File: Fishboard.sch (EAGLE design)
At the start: 21 parts, among them J3 B1, J4 B2, J5 B3, J7 B4, Q1 TIP120, Q2 TIP120, Q3 TIP120

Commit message: Reorganized schematics
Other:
- note added: "I2C Header for SSD1306"
- note added: "Input buttons"
- note added: "Oak Headers"
- note added: "Transistor Logic"
- moved on the sheet: J1, J10, J2, J4, J6, J8, J9, Q1, Q2, Q3, R1, R2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

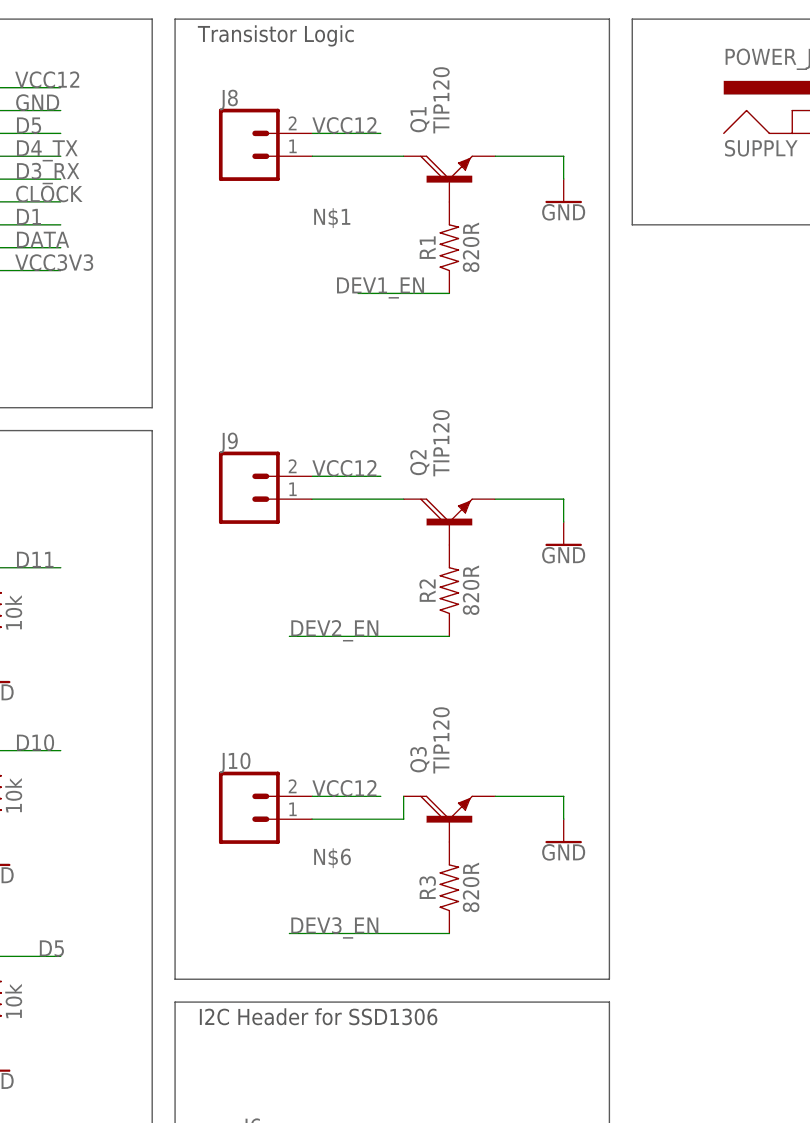
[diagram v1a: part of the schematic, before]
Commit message: Switched the TIP120 with a logic level MOSFET (FQP30N06L). The current limiting resistors have been replaced with pulldowns.
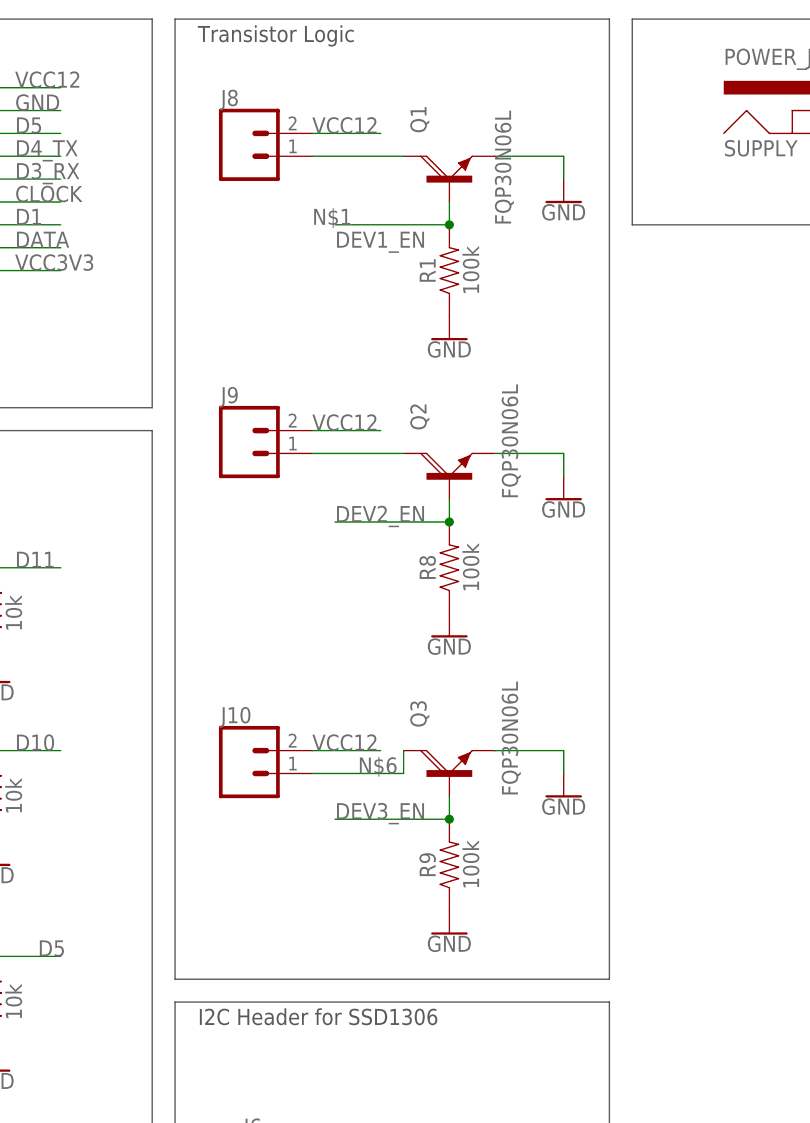
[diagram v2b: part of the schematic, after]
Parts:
- removed R2, R3: 820R, SparkFun-Resistors:1KOHM-HORIZ-1/4W-5%
- added R8, R9: 100k, SparkFun-Resistors:100KOHM-HORIZ-1/4W-5%
- Q1, Q2, Q3: value TIP120 -> FQP30N06L
- R1: value 820R -> 100k; device SparkFun-Resistors:1KOHM-HORIZ-1/4W-5% -> SparkFun-Resistors:100KOHM-HORIZ-1/4W-5%
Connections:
- removed net N$2: Q1.B, R1.2
- removed net N$3: Q2.B, R2.2
- removed net N$4: Q3.B, R3.2
- net DEV1_EN: now also Q1.B, R1.2; no longer R1.1
- net DEV2_EN: now also Q2.B, R8.2; no longer R2.1
- net DEV3_EN: now also Q3.B, R9.2; no longer R3.1
- net GND: now also R1.1, R8.1, R9.1
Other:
- moved on the sheet: J10, J9, Q2, Q3, R1
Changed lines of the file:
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@@
 <part name="GND1" library="SparkFun-PowerSymbols" deviceset="GND" device=""/>
 <part name="GND2" library="SparkFun-PowerSymbols" deviceset="GND" device=""/>
-<part name="Q1" library="transistor-power" deviceset="TIP120" device="" value="TIP120"/>
-<part name="Q2" library="transistor-power" deviceset="TIP120" device="" value="TIP120"/>
-<part name="Q3" library="transistor-power" deviceset="TIP120" device="" value="TIP120"/>
+<part name="Q1" library="transistor-power" deviceset="TIP120" device="" value="FQP30N06L"/>
+<part name="Q2" library="transistor-power" deviceset="TIP120" device="" value="FQP30N06L"/>
+<part name="Q3" library="transistor-power" deviceset="TIP120" device="" value="FQP30N06L"/>
 <part name="GND5" library="SparkFun-PowerSymbols" deviceset="GND" device=""/>
 <part name="GND6" library="SparkFun-PowerSymbols" deviceset="GND" device=""/>
-<part name="R1" library="SparkFun-Resistors" deviceset="1KOHM" device="-HORIZ-1/4W-5%" value="820R"/>
-<part name="R2" library="SparkFun-Resistors" deviceset="1KOHM" device="-HORIZ-1/4W-5%" value="820R"/>
-<part name="R3" library="SparkFun-Resistors" deviceset="1KOHM" device="-HORIZ-1/4W-5%" value="820R"/>
 <part name="J3" library="SparkFun-Connectors" deviceset="CONN_02" device="LOCK" value="B1"/>
 <part name="J4" library="SparkFun-Connectors" deviceset="CONN_02" device="LOCK" value="B2"/>
@@
 <part name="J9" library="SparkFun-Connectors" deviceset="CONN_02" device="PTH3"/>
 <part name="J10" library="SparkFun-Connectors" deviceset="CONN_02" device="PTH3"/>
+<part name="R1" library="SparkFun-Resistors" deviceset="100KOHM" device="-HORIZ-1/4W-5%" value="100k"/>
+<part name="R8" library="SparkFun-Resistors" deviceset="100KOHM" device="-HORIZ-1/4W-5%" value="100k"/>
+<part name="R9" library="SparkFun-Resistors" deviceset="100KOHM" device="-HORIZ-1/4W-5%" value="100k"/>
+<part name="GND9" library="SparkFun-PowerSymbols" deviceset="GND" device=""/>
+<part name="GND10" library="SparkFun-PowerSymbols" deviceset="GND" device=""/>
+<part name="GND11" library="SparkFun-PowerSymbols" deviceset="GND" device=""/>
 </parts>
 <sheets>
@@
 <instance part="GND1" gate="1" x="142.24" y="73.66"/>
 <instance part="GND2" gate="1" x="104.14" y="71.12"/>
-<instance part="Q1" gate="1" x="91.44" y="73.66" rot="R90"/>
-<instance part="Q2" gate="1" x="91.44" y="35.56" rot="R90"/>
-<instance part="Q3" gate="1" x="91.44" y="2.54" rot="R90"/>
-<instance part="GND5" gate="1" x="104.14" y="33.02"/>
-<instance part="GND6" gate="1" x="104.14" y="0"/>
-<instance part="R1" gate="G$1" x="91.44" y="66.04" rot="R90"/>
-<instance part="R2" gate="G$1" x="91.44" y="27.94" rot="R90"/>
-<instance part="R3" gate="G$1" x="91.44" y="-5.08" rot="R90"/>
+<instance part="Q1" gate="1" x="91.44" y="73.66" smashed="yes" rot="R90">
+<attribute name="NAME" x="88.9" y="78.74" size="1.778" layer="95" rot="R90"/>
+<attribute name="VALUE" x="96.52" y="81.28" size="1.778" layer="96" rot="R270"/>
+</instance>
+<instance part="Q2" gate="1" x="91.44" y="40.64" smashed="yes" rot="R90">
+<attribute name="NAME" x="88.9" y="45.72" size="1.778" layer="95" rot="R90"/>
+<attribute name="VALUE" x="99.06" y="38.1" size="1.778" layer="96" rot="R90"/>
+</instance>
+<instance part="Q3" gate="1" x="91.44" y="7.62" smashed="yes" rot="R90">
+<attribute name="NAME" x="88.9" y="12.7" size="1.778" layer="95" rot="R90"/>
+<attribute name="VALUE" x="99.06" y="5.08" size="1.778" layer="96" rot="R90"/>
+</instance>
+<instance part="GND5" gate="1" x="104.14" y="38.1"/>
+<instance part="GND6" gate="1" x="104.14" y="5.08"/>
 <instance part="J3" gate="G$1" x="10.16" y="27.94"/>
 <instance part="J4" gate="G$1" x="10.16" y="7.62"/>
@@
 <instance part="GND8" gate="1" x="40.64" y="-48.26"/>
 <instance part="J8" gate="G$1" x="68.58" y="76.2"/>
-<instance part="J9" gate="G$1" x="68.58" y="38.1"/>
-<instance part="J10" gate="G$1" x="68.58" y="2.54"/>
+<instance part="J9" gate="G$1" x="68.58" y="43.18"/>
+<instance part="J10" gate="G$1" x="68.58" y="7.62"/>
+<instance part="R1" gate="G$1" x="91.44" y="63.5" rot="R90"/>
+<instance part="R8" gate="G$1" x="91.44" y="30.48" rot="R90"/>
+<instance part="R9" gate="G$1" x="91.44" y="-2.54" rot="R90"/>
+<instance part="GND9" gate="1" x="91.44" y="55.88"/>
+<instance part="GND10" gate="1" x="91.44" y="22.86"/>
+<instance part="GND11" gate="1" x="91.44" y="-10.16"/>
 </instances>
 <busses>
@@
 <pinref part="Q2" gate="1" pin="E"/>
 <pinref part="GND5" gate="1" pin="GND"/>
-<wire x1="96.52" y1="38.1" x2="104.14" y2="38.1" width="0.1524" layer="91"/>
-<wire x1="104.14" y1="38.1" x2="104.14" y2="35.56" width="0.1524" layer="91"/>
+<wire x1="96.52" y1="43.18" x2="104.14" y2="43.18" width="0.1524" layer="91"/>
+<wire x1="104.14" y1="43.18" x2="104.14" y2="40.64" width="0.1524" layer="91"/>
 </segment>
 <segment>
@@
 <pinref part="Q3" gate="1" pin="E"/>
 <pinref part="GND6" gate="1" pin="GND"/>
-<wire x1="96.52" y1="5.08" x2="104.14" y2="5.08" width="0.1524" layer="91"/>
-<wire x1="104.14" y1="5.08" x2="104.14" y2="2.54" width="0.1524" layer="91"/>
+<wire x1="96.52" y1="10.16" x2="104.14" y2="10.16" width="0.1524" layer="91"/>
+<wire x1="104.14" y1="10.16" x2="104.14" y2="7.62" width="0.1524" layer="91"/>
 </segment>
 <segment>
@@
 <label x="91.44" y="-43.18" size="1.778" layer="95"/>
 </segment>
+<segment>
+<pinref part="R1" gate="G$1" pin="1"/>
+<pinref part="GND9" gate="1" pin="GND"/>
+</segment>
+<segment>
+<pinref part="R8" gate="G$1" pin="1"/>
+<pinref part="GND10" gate="1" pin="GND"/>
+</segment>
+<segment>
+<pinref part="R9" gate="G$1" pin="1"/>
+<pinref part="GND11" gate="1" pin="GND"/>
+</segment>
 </net>
 <net name="VCC12" class="0">
@@
 </segment>
 <segment>
-<label x="76.2" y="40.64" size="1.778" layer="95"/>
+<label x="76.2" y="45.72" size="1.778" layer="95"/>
 <pinref part="J9" gate="G$1" pin="2"/>
-<wire x1="76.2" y1="40.64" x2="83.82" y2="40.64" width="0.1524" layer="91"/>
-</segment>
-<segment>
-<wire x1="76.2" y1="5.08" x2="83.82" y2="5.08" width="0.1524" layer="91"/>
-<label x="76.2" y="5.08" size="1.778" layer="95"/>
+<wire x1="76.2" y1="45.72" x2="83.82" y2="45.72" width="0.1524" layer="91"/>
+</segment>
+<segment>
+<wire x1="76.2" y1="10.16" x2="83.82" y2="10.16" width="0.1524" layer="91"/>
+<label x="76.2" y="10.16" size="1.778" layer="95"/>
 <pinref part="J10" gate="G$1" pin="2"/>
 </segment>
@@
 </segment>
 </net>
-<net name="N$2" class="0">
-<segment>
+<net name="DEV1_EN" class="0">
+<segment>
+<wire x1="91.44" y1="68.58" x2="78.74" y2="68.58" width="0.1524" layer="91"/>
+<label x="78.74" y="66.04" size="1.778" layer="95"/>
+<pinref part="R1" gate="G$1" pin="2"/>
 <pinref part="Q1" gate="1" pin="B"/>
-<pinref part="R1" gate="G$1" pin="2"/>
-</segment>
-</net>
-<net name="N$3" class="0">
-<segment>
-<pinref part="Q2" gate="1" pin="B"/>
-<pinref part="R2" gate="G$1" pin="2"/>
-</segment>
-</net>
-<net name="N$4" class="0">
-<segment>
-<pinref part="Q3" gate="1" pin="B"/>
-<pinref part="R3" gate="G$1" pin="2"/>
-</segment>
-</net>
-<net name="DEV1_EN" class="0">
-<segment>
-<pinref part="R1" gate="G$1" pin="1"/>
-<wire x1="91.44" y1="60.96" x2="81.28" y2="60.96" width="0.1524" layer="91"/>
-<label x="78.74" y="60.96" size="1.778" layer="95"/>
+<wire x1="91.44" y1="71.12" x2="91.44" y2="68.58" width="0.1524" layer="91"/>
+<junction x="91.44" y="68.58"/>
 </segment>
 <segment>
@@
 <net name="DEV2_EN" class="0">
 <segment>
-<pinref part="R2" gate="G$1" pin="1"/>
-<wire x1="91.44" y1="22.86" x2="73.66" y2="22.86" width="0.1524" layer="91"/>
-<label x="73.66" y="22.86" size="1.778" layer="95"/>
+<wire x1="91.44" y1="35.56" x2="78.74" y2="35.56" width="0.1524" layer="91"/>
+<label x="78.74" y="35.56" size="1.778" layer="95"/>
+<pinref part="R8" gate="G$1" pin="2"/>
+<pinref part="Q2" gate="1" pin="B"/>
+<wire x1="91.44" y1="38.1" x2="91.44" y2="35.56" width="0.1524" layer="91"/>
+<junction x="91.44" y="35.56"/>
 </segment>
 <segment>
@@
 <net name="DEV3_EN" class="0">
 <segment>
-<pinref part="R3" gate="G$1" pin="1"/>
-<wire x1="91.44" y1="-10.16" x2="73.66" y2="-10.16" width="0.1524" layer="91"/>
-<label x="73.66" y="-10.16" size="1.778" layer="95"/>
+<wire x1="91.44" y1="2.54" x2="78.74" y2="2.54" width="0.1524" layer="91"/>
+<label x="78.74" y="2.54" size="1.778" layer="95"/>
+<pinref part="R9" gate="G$1" pin="2"/>
+<pinref part="Q3" gate="1" pin="B"/>
+<wire x1="91.44" y1="2.54" x2="91.44" y2="5.08" width="0.1524" layer="91"/>
+<junction x="91.44" y="2.54"/>
 </segment>
 <segment>
@@
 <segment>
 <pinref part="Q3" gate="1" pin="C"/>
-<wire x1="76.2" y1="2.54" x2="86.36" y2="2.54" width="0.1524" layer="91"/>
-<wire x1="86.36" y1="2.54" x2="86.36" y2="5.08" width="0.1524" layer="91"/>
-<label x="76.2" y="-2.54" size="1.778" layer="95"/>
+<wire x1="76.2" y1="7.62" x2="86.36" y2="7.62" width="0.1524" layer="91"/>
+<wire x1="86.36" y1="7.62" x2="86.36" y2="10.16" width="0.1524" layer="91"/>
+<label x="81.28" y="7.62" size="1.778" layer="95"/>
 <pinref part="J10" gate="G$1" pin="1"/>
 </segment>
@@
 <net name="N$5" class="0">
 <segment>
-<wire x1="76.2" y1="38.1" x2="86.36" y2="38.1" width="0.1524" layer="91"/>
+<wire x1="76.2" y1="43.18" x2="86.36" y2="43.18" width="0.1524" layer="91"/>
 <pinref part="Q2" gate="1" pin="C"/>
 <pinref part="J9" gate="G$1" pin="1"/>

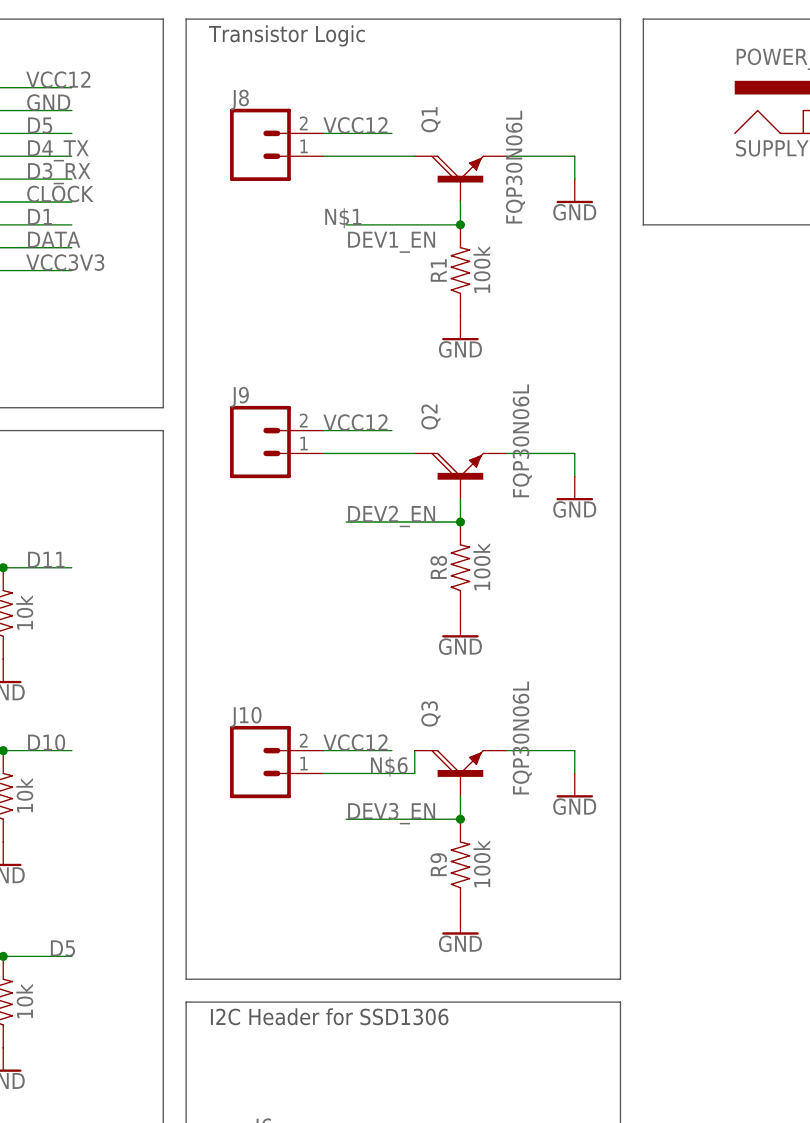
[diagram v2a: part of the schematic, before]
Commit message: Replaced TIP120 part with custom part so that we can correctly route it.
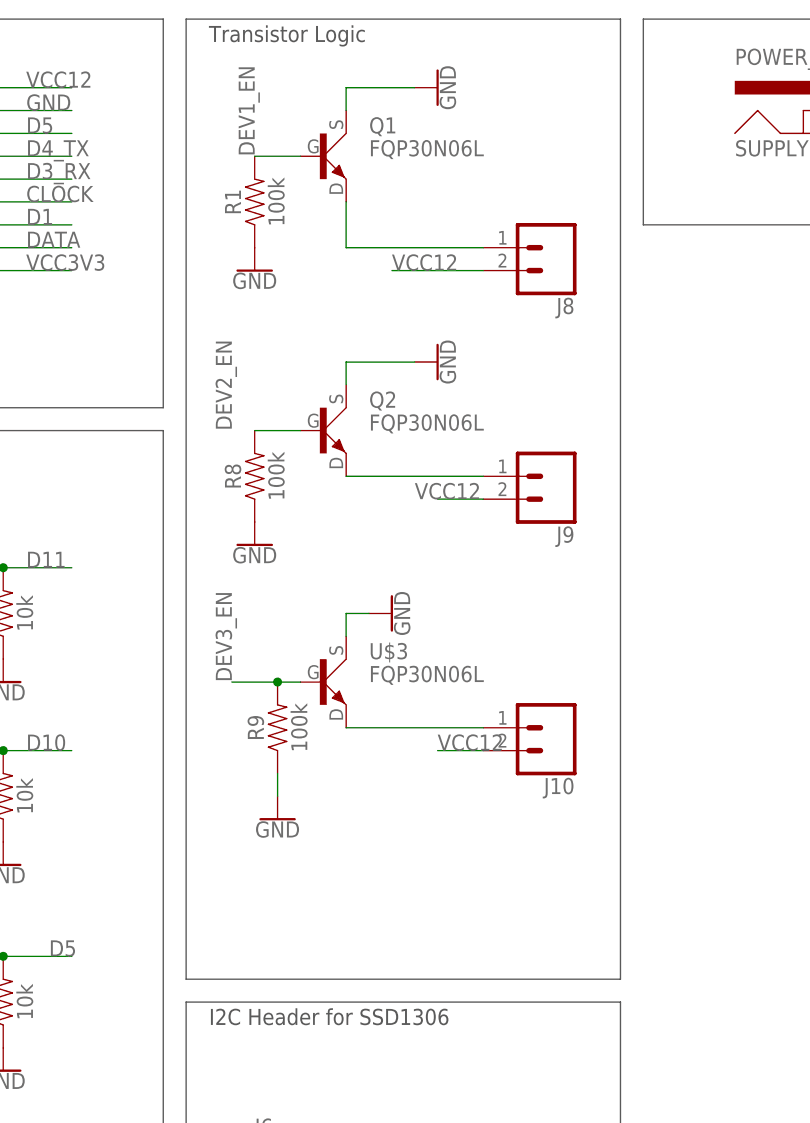
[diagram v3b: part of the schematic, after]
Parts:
- removed Q3: FQP30N06L, transistor-power:TIP120
- added U$3: FQP30N06L, fishlib:FQP30N06L
- Q1, Q2: device transistor-power:TIP120 -> fishlib:FQP30N06L
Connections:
- removed net N$5: J9.1, Q2.C
- removed net N$6: J10.1, Q3.C
- new net N$2: J8.1, Q1.2
- new net N$4: J10.1, U$3.2
- net DEV1_EN: now also Q1.1; no longer Q1.B
- net DEV2_EN: now also Q2.1; no longer Q2.B
- net DEV3_EN: now also U$3.1; no longer Q3.B
- net GND: now also Q1.3, Q2.3, U$3.3; no longer Q1.E, Q2.E, Q3.E
- net N$1: now also J9.1, Q2.2; no longer J8.1, Q1.C
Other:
- moved on the sheet: J10, J8, J9, R1, R8, R9
